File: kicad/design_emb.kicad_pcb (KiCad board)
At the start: 2 copper layers, 110 parts, among them J1 Conn_01x03, J2 Barrel_Jack, J3 USB_A, J4 Conn_01x03, J5 Conn_02x11_Counter_Clockwise, J6 Conn_02x10_Counter_Clockwise, J7 Screw_Terminal_01x02, J8 Screw_Terminal_01x02, K1 SANYOU_SRD_Form_C, K2 SANYOU_SRD_Form_C, Q1 MMBT3904, Q2 MMBT3904, U1 SRX.X.TCT, U10 S25FL116KOXNFIQ-11, U2 SRX.X.TCT, U3 STM32F446ZETx, U4 ICE40HX1K, U5 TLV1117LV33DCYR, U6 TLV1117LV33DCYR, U7 TLV1117LV12DCYR, U8 OMEGA2, U9 RCLAMP0502B

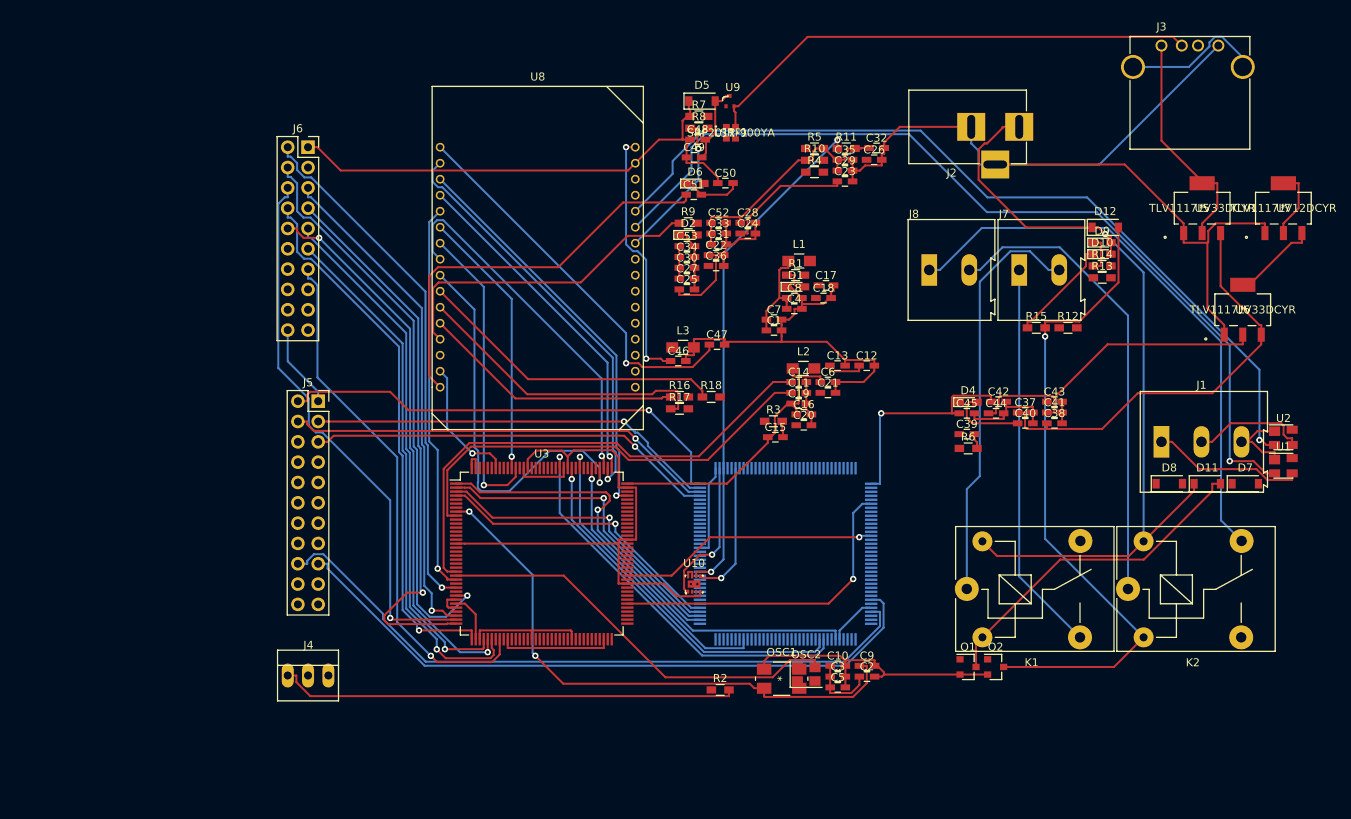
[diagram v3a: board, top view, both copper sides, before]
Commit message: arreglo pines FPGA compatibilidad STM32
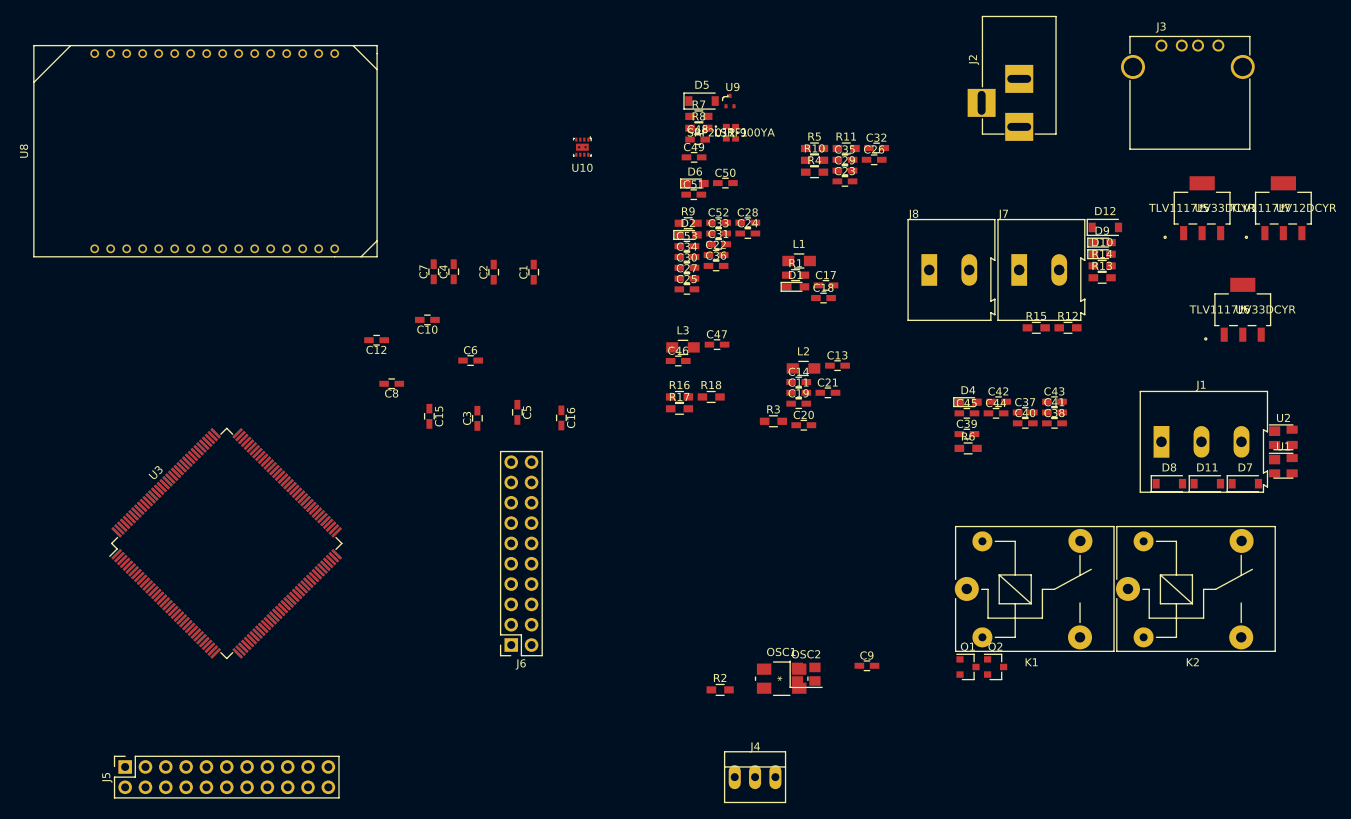
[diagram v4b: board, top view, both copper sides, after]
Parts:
- moved U4 69.9 mm to (52.1, 135.9), turned to 45 degrees
- moved C2 68.8 mm to (85.4, 102.0), turned to 90 degrees
- moved J6 67.2 mm to (87.6, 148.6), turned to 180 degrees
- moved C10 67.1 mm to (77.2, 108.0), turned to 180 degrees
- moved C12 61.3 mm to (70.8, 110.5), turned to 180 degrees
- moved J4 57.3 mm to (115.6, 165.1)
- moved U10 56.4 mm to (96.5, 86.4), turned to 180 degrees
- moved C3 55.4 mm to (83.4, 120.2), turned to 90 degrees
- moved C5 52.8 mm to (88.4, 119.5), turned to 270 degrees
- moved J5 51.7 mm to (39.4, 163.8), turned to 90 degrees
- moved C8 51.5 mm to (72.7, 115.9), turned to 180 degrees
- moved U8 45.0 mm to (35.6, 99.1), turned to 90 degrees
- moved C6 44.7 mm to (82.5, 113.0)
- moved C15 43.3 mm to (77.4, 120.0), turned to 270 degrees
- moved C7 43.0 mm to (77.9, 101.9), turned to 90 degrees
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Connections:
- net /sheet3/FMCNBL0 renamed Net-(U4-Pad112)
- net /sheet3/FMCNBL1 renamed Net-(U4-Pad113)
- J5 pad 10: /sheet3/GPIO18 -> /sheet3/GPIO7
- J5 pad 11: /sheet3/GPIO19 -> /sheet3/GPIO8
- J5 pad 13: /sheet3/GPIO8 -> /sheet3/GPIO10
- J5 pad 14: /sheet3/GPIO7 -> /sheet3/GPIO11
- J5 pad 15: /sheet3/GPIO6 -> /sheet3/GPIO12
- J5 pad 16: /sheet3/GPIO5 -> /sheet3/GPIO13
- J5 pad 17: /sheet3/GPIO4 -> /sheet3/GPIO14
- J5 pad 18: /sheet3/GPIO3 -> /sheet3/GPIO15
- J5 pad 19: /sheet3/GPIO2 -> /sheet3/GPIO16
- J5 pad 2: /sheet3/GPIO10 -> /Sheet4/+3V3_FPGA
- J5 pad 20: /sheet3/GPIO1 -> /sheet3/GPIO17
- J5 pad 21: /sheet3/GPIO0 -> /sheet3/GPIO18
- J5 pad 22: /Sheet4/+3V3_FPGA -> /sheet3/GPIO19
- J5 pad 3: /sheet3/GPIO11 -> /sheet3/GPIO0
- J5 pad 4: /sheet3/GPIO12 -> /sheet3/GPIO1
- J5 pad 5: /sheet3/GPIO13 -> /sheet3/GPIO2
- J5 pad 6: /sheet3/GPIO14 -> /sheet3/GPIO3
- J5 pad 7: /sheet3/GPIO15 -> /sheet3/GPIO4
- J5 pad 8: /sheet3/GPIO16 -> /sheet3/GPIO5
- J5 pad 9: /sheet3/GPIO17 -> /sheet3/GPIO6
- J6 pad 10: /Sheet1/USR9 -> /Sheet1/USR8
- J6 pad 11: /Sheet1/USR10 -> /Sheet1/USR9
- J6 pad 12: /Sheet1/USR11 -> /Sheet1/USR10
- J6 pad 13: /Sheet1/USR12 -> /Sheet1/USR11
- J6 pad 14: /Sheet1/USR13 -> /Sheet1/USR12
- J6 pad 15: /Sheet1/USR14 -> /Sheet1/USR13
- J6 pad 16: /Sheet1/USR15 -> /Sheet1/USR14
- J6 pad 17: /Sheet1/USR16 -> /Sheet1/USR15
- J6 pad 18: /Sheet1/USR17 -> /Sheet1/USR16
- J6 pad 19: /Sheet1/USR18 -> /Sheet1/USR17
- J6 pad 2: /Sheet1/USR1 -> GND
- J6 pad 20: GND -> /Sheet1/USR18
- J6 pad 3: /Sheet1/USR2 -> /Sheet1/USR1
- J6 pad 4: /Sheet1/USR3 -> /Sheet1/USR2
- J6 pad 5: /Sheet1/USR4 -> /Sheet1/USR3
- J6 pad 6: /Sheet1/USR5 -> /Sheet1/USR4
- J6 pad 7: /Sheet1/USR6 -> /Sheet1/USR5
- J6 pad 8: /Sheet1/USR7 -> /Sheet1/USR6
- J6 pad 9: /Sheet1/USR8 -> /Sheet1/USR7
- R10 pad 2: /sheet3/SPI0 -> /Sheet2/SPI0
- R11 pad 1: /sheet3/SPI1 -> /Sheet2/SPI1
- R12 pad 1: Net-(R12-Pad1) -> Net-(Q1-Pad1)
- R13 pad 1: Net-(R13-Pad1) -> Net-(Q2-Pad1)
- U10 pad 1: /sheet3/SPI0 -> /Sheet2/SPI0
- U10 pad 2: /sheet3/SPI2 -> /Sheet2/SPI2
- U10 pad 5: /sheet3/SPI3 -> /Sheet2/SPI3
- U10 pad 6: /sheet3/SPI1 -> /Sheet2/SPI1
- U3 pad 100: Net-(U3-Pad100) -> /Sheet1/USR16
- U3 pad 101: Net-(U3-Pad101) -> /Sheet1/USR17
- U3 pad 102: Net-(U3-Pad102) -> /Sheet1/USR18
- U3 pad 27: /Sheet1/USR1 -> Net-(U3-Pad27)
- U3 pad 28: /Sheet1/USR2 -> Net-(U3-Pad28)
- U3 pad 29: /Sheet1/USR3 -> Net-(U3-Pad29)
- U3 pad 34: /Sheet1/USR4 -> Net-(U3-Pad34)
- U3 pad 35: /Sheet1/USR5 -> Net-(U3-Pad35)
- U3 pad 36: /Sheet1/USR6 -> Net-(U3-Pad36)
- U3 pad 37: /Sheet1/USR7 -> /Sheet1/USR1
- U3 pad 40: /Sheet1/USR8 -> /Sheet1/USR2
- U3 pad 41: /Sheet1/USR9 -> /Sheet1/USR3
- U3 pad 42: /Sheet1/USR10 -> /Sheet1/USR4
- U3 pad 43: /Sheet1/USR11 -> /Sheet1/USR5
- U3 pad 44: /Sheet1/USR12 -> Net-(U3-Pad44)
- U3 pad 46: /Sheet1/USR14 -> Net-(U3-Pad46)
- U3 pad 69: /Sheet1/USR13 -> /Sheet1/USR6
- U3 pad 70: /Sheet1/USR14 -> /Sheet1/USR7
- U3 pad 73: /Sheet1/USR15 -> /Sheet1/USR8
- U3 pad 74: /Sheet1/USR16 -> /Sheet1/USR9
- U3 pad 75: /Sheet1/USR17 -> /Sheet1/USR10
- U3 pad 76: /Sheet1/USR18 -> /Sheet1/USR11
- U3 pad 96: Net-(U3-Pad96) -> /Sheet1/USR12
- U3 pad 97: Net-(U3-Pad97) -> /Sheet1/USR13
- U3 pad 98: Net-(U3-Pad98) -> /Sheet1/USR14
- U3 pad 99: Net-(U3-Pad99) -> /Sheet1/USR15
- U4 pad 1: /sheet3/GPIO0 -> /Sheet1/FMCA23
- U4 pad 10: /sheet3/GPIO7 -> Net-(U4-Pad10)
- U4 pad 102: /Sheet1/FMCA22 -> Net-(U4-Pad102)
- U4 pad 104: /Sheet1/FMCA21 -> Net-(U4-Pad104)
- U4 pad 105: /Sheet1/FMCA20 -> Net-(U4-Pad105)
- U4 pad 106: /Sheet1/FMCA19 -> Net-(U4-Pad106)
- U4 pad 107: /Sheet1/FMCA23 -> Net-(U4-Pad107)
- U4 pad 11: /sheet3/GPIO8 -> Net-(U4-Pad11)
- U4 pad 114: Net-(U4-Pad114) -> /Sheet1/FMCAD3
- U4 pad 115: /Sheet1/CTRL0 -> /Sheet1/FMCAD2
- U4 pad 116: /Sheet1/CTRL1 -> Net-(U4-Pad116)
- U4 pad 117: Net-(U4-Pad117) -> /Sheet1/CTRL1
- U4 pad 118: Net-(U4-Pad118) -> /Sheet1/CTRL2
- U4 pad 119: Net-(U4-Pad119) -> /Sheet1/CTRL3
- U4 pad 12: /sheet3/GPIO9 -> Net-(U4-Pad12)
- U4 pad 120: Net-(U4-Pad120) -> /Sheet1/CTRL4
- U4 pad 121: Net-(U4-Pad121) -> /Sheet1/CTRL5
- U4 pad 134: /Sheet1/CTRL2 -> Net-(U4-Pad134)
- U4 pad 135: /Sheet1/CTRL3 -> Net-(U4-Pad135)
- U4 pad 136: /Sheet1/CTRL4 -> Net-(U4-Pad136)
- U4 pad 137: /Sheet1/CTRL5 -> /Sheet1/CTRL0
- U4 pad 138: /Sheet1/FMCAD3 -> Net-(U4-Pad138)
- U4 pad 139: /Sheet1/FMCAD2 -> Net-(U4-Pad139)
- U4 pad 141: Net-(U4-Pad141) -> /Sheet1/FMCNBL0
- U4 pad 142: Net-(U4-Pad142) -> /Sheet1/FMCNBL1
- U4 pad 19: Net-(U4-Pad19) -> /sheet3/GPIO0
- U4 pad 2: /sheet3/GPIO1 -> /Sheet1/FMCA22
- U4 pad 22: /Sheet1/FMCAD1 -> /sheet3/GPIO1
- U4 pad 23: /Sheet1/FMCAD0 -> /sheet3/GPIO2
- U4 pad 24: Net-(U4-Pad24) -> /sheet3/GPIO3
- U4 pad 25: /Sheet1/FMCA18 -> /sheet3/GPIO4
- U4 pad 26: /Sheet1/FMCA17 -> /sheet3/GPIO5
- U4 pad 28: /Sheet1/FMCA16 -> /sheet3/GPIO6
- U4 pad 29: /Sheet1/FMCAD15 -> /sheet3/GPIO7
- U4 pad 3: /sheet3/GPIO2 -> /Sheet1/FMCA19
- U4 pad 31: /Sheet1/FMCAD14 -> /sheet3/GPIO8
- U4 pad 32: /Sheet1/FMCAD13 -> /sheet3/GPIO9
- U4 pad 33: Net-(U4-Pad33) -> /sheet3/GPIO10
- U4 pad 34: Net-(U4-Pad34) -> /sheet3/GPIO11
- U4 pad 37: Net-(U4-Pad37) -> /sheet3/GPIO12
- U4 pad 38: Net-(U4-Pad38) -> /sheet3/GPIO13
- U4 pad 39: Net-(U4-Pad39) -> /sheet3/GPIO14
- U4 pad 4: /sheet3/GPIO3 -> /Sheet1/FMCA20
- U4 pad 41: /Sheet1/FMCAD12 -> /sheet3/GPIO15
- U4 pad 42: /Sheet1/FMCAD11 -> /sheet3/GPIO16
- U4 pad 43: /Sheet1/FMCAD10 -> /sheet3/GPIO17
- U4 pad 44: /Sheet1/FMCAD9 -> /sheet3/GPIO18
- U4 pad 45: /Sheet1/FMCAD8 -> /sheet3/GPIO19
- U4 pad 47: /Sheet1/FMCAD7 -> Net-(U4-Pad47)
- U4 pad 48: /Sheet1/FMCAD6 -> Net-(U4-Pad48)
- U4 pad 49: /Sheet1/FMCAD5 -> Net-(U4-Pad49)
- U4 pad 50: /Sheet1/FMCAD4 -> Net-(U4-Pad50)
- U4 pad 56: Net-(U4-Pad56) -> /Sheet1/FMCAD4
- U4 pad 58: Net-(U4-Pad58) -> /Sheet1/FMCAD5
- U4 pad 60: Net-(U4-Pad60) -> /Sheet1/FMCAD6
- U4 pad 61: Net-(U4-Pad61) -> /Sheet1/FMCAD7
- U4 pad 62: Net-(U4-Pad62) -> /Sheet1/FMCAD8
- U4 pad 67: /sheet3/SPI3 -> /Sheet2/SPI3
- U4 pad 68: /sheet3/SPI2 -> /Sheet2/SPI2
- U4 pad 7: /sheet3/GPIO4 -> /Sheet1/FMCA21
- U4 pad 70: /sheet3/SPI1 -> /Sheet2/SPI1
- U4 pad 71: /sheet3/SPI0 -> /Sheet2/SPI0
- U4 pad 73: /sheet3/GPIO10 -> /Sheet1/FMCAD9
- U4 pad 74: /sheet3/GPIO11 -> /Sheet1/FMCAD10
- U4 pad 75: /sheet3/GPIO12 -> /Sheet1/FMCAD11
- U4 pad 76: /sheet3/GPIO13 -> /Sheet1/FMCAD12
- U4 pad 78: /sheet3/GPIO14 -> /Sheet1/FMCAD13
- U4 pad 79: /sheet3/GPIO15 -> /Sheet1/FMCAD14
- U4 pad 8: /sheet3/GPIO5 -> Net-(U4-Pad8)
- U4 pad 80: /sheet3/GPIO16 -> /Sheet1/FMCAD15
- U4 pad 81: /sheet3/GPIO17 -> /Sheet1/FMCA16
- U4 pad 87: /sheet3/GPIO18 -> /Sheet1/FMCAD0
- U4 pad 88: /sheet3/GPIO19 -> /Sheet1/FMCAD1
- U4 pad 9: /sheet3/GPIO6 -> Net-(U4-Pad9)
- U4 pad 90: Net-(U4-Pad90) -> /Sheet1/FMCA17
- U4 pad 91: Net-(U4-Pad91) -> /Sheet1/FMCA18
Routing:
- net GND: track 367.4 -> 0.00 mm
- net VDD: track 194.0 -> 0.00 mm
- net /SERIAL_RX: track 112.5 -> 0.00 mm, vias 1 -> 0
- net /SERIAL_TX: track 106.4 -> 0.00 mm, vias 1 -> 0
- net +5VA: track 103.7 -> 0.00 mm, vias 1 -> 0
- net /Sheet4/+3V3_FPGA: track 99.5 -> 0.00 mm
- net /sheet3/GPIO3: track 84.1 -> 0.00 mm
- net /sheet3/GPIO4: track 83.1 -> 0.00 mm
- net Net-(D12-Pad2): track 81.7 -> 0.00 mm, vias 1 -> 0
- net /Sheet1/USR3: track 71.5 -> 0.00 mm, vias 1 -> 0
- net /Sheet1/OSC32_IN: track 71.1 -> 0.00 mm, vias 2 -> 0
- net Net-(J8-Pad1): track 70.5 -> 0.00 mm
- net /Sheet1/USR6: track 69.8 -> 0.00 mm, vias 1 -> 0
- net /Sheet1/USR5: track 69.1 -> 0.00 mm, vias 1 -> 0
- net /Sheet1/USR9: track 68.8 -> 0.00 mm, vias 2 -> 0
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
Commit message: design_emb.kicad_pcb
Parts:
- moved D7 108.1 mm to (72.4, 143.5), turned to 180 degrees
- moved D8 98.3 mm to (72.4, 141.0), turned to 180 degrees
- moved C17 98.3 mm to (43.2, 154.9), turned to 270 degrees
- moved C9 97.8 mm to (34.3, 148.6), turned to 90 degrees
- moved C14 96.4 mm to (35.6, 154.9), turned to 90 degrees
- moved C11 85.2 mm to (44.5, 148.6), turned to 270 degrees
- moved OSC2 85.1 mm to (39.4, 154.8)
- moved J2 84.2 mm to (104.1, 153.7)
- moved OSC1 82.2 mm to (39.4, 148.6)
- moved D11 63.9 mm to (116.0, 153.7)
- moved J4 43.8 mm to (72.4, 157.5), turned to 90 degrees
- moved R2 40.5 mm to (73.7, 160.0), turned to 180 degrees
- moved J1 38.2 mm to (171.4, 161.3)
- moved LSRF1 24.9 mm to (90.9, 78.7)
- moved U9 24.8 mm to (90.9, 74.3)
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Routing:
- net /sheet3/GPIO1: track 0.00 -> 21.3 mm
- net /sheet3/GPIO3: track 0.00 -> 20.5 mm
- net /sheet3/GPIO5: track 0.00 -> 19.8 mm
- net /sheet3/GPIO17: track 0.00 -> 19.5 mm
- net /sheet3/GPIO0: track 0.00 -> 19.3 mm
- net /sheet3/GPIO7: track 0.00 -> 19.1 mm
- net /sheet3/GPIO9: track 0.00 -> 18.5 mm
- net /sheet3/GPIO11: track 0.00 -> 18.3 mm
- net /sheet3/GPIO15: track 0.00 -> 18.2 mm
- net /sheet3/GPIO2: track 0.00 -> 17.5 mm
- net /sheet3/GPIO18: track 0.00 -> 17.3 mm
- net /sheet3/GPIO4: track 0.00 -> 17.0 mm
- net /sheet3/GPIO13: track 0.00 -> 16.5 mm
- net /sheet3/GPIO6: track 0.00 -> 16.4 mm
- net /sheet3/GPIO16: track 0.00 -> 15.8 mm
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
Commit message: ruteo
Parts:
- moved C14 9.16 mm to (43.2, 149.9), turned to 45 degrees
- moved C9 8.98 mm to (33.0, 139.7), turned to 45 degrees
- moved OSC2 6.75 mm to (45.7, 152.4), turned to 315 degrees
- moved J6 5.80 mm to (87.6, 148.3)
- moved OSC1 5.68 mm to (36.8, 143.5), turned to 315 degrees
- moved C17 5.08 mm to (48.3, 154.9), turned to 225 degrees
- moved C11 4.02 mm to (40.6, 147.3), turned to 225 degrees
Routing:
- net /Sheet1/OSC32_IN: track 0.00 -> 10.9 mm
- net /Sheet1/OSC_OUT: track 0.00 -> 10.5 mm
- net /Sheet1/OSC_IN: track 0.00 -> 9.50 mm
- net /Sheet1/OSC32_OUT: track 0.00 -> 8.19 mm
- net /Sheet1/FMCAD9: track 0.00 -> 7.53 mm, vias 0 -> 1
- net /Sheet1/FMCAD10: track 0.00 -> 7.34 mm, vias 0 -> 1
- net /Sheet1/FMCAD12: track 0.00 -> 7.16 mm, vias 0 -> 1
- net /Sheet1/FMCAD11: track 0.00 -> 7.13 mm, vias 0 -> 1
- net /Sheet1/FMCA22: track 11.1 -> 4.38 mm
- net /Sheet1/FMCA21: track 0.00 -> 5.85 mm, vias 0 -> 1
- net /Sheet1/FMCAD8: track 0.00 -> 5.62 mm, vias 0 -> 1
- net /Sheet1/FMCAD6: track 0.00 -> 5.26 mm, vias 0 -> 1
- net /Sheet1/FMCAD4: track 0.00 -> 4.20 mm, vias 0 -> 1
- net /Sheet1/FMCAD5: track 0.00 -> 3.86 mm, vias 0 -> 1
- net /Sheet1/FMCAD7: track 0.00 -> 3.83 mm, vias 0 -> 1
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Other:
- net class signals added: clearance 0.15, trace_width 0.15, via_dia 0.8, via_drill 0.4
- rule trace_min: 0.2 -> 0.15

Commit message: ruteo
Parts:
- moved K1 146.1 mm to (267.4, 113.5), turned to 180 degrees
- moved J2 135.8 mm to (206.6, 64.6)
- moved K2 132.1 mm to (267.6, 95.1), turned to 180 degrees
- moved D7 105.1 mm to (177.2, 150.6)
- moved D8 105.0 mm to (177.3, 145.9)
- moved J4 101.2 mm to (172.7, 171.5)
- moved R2 98.8 mm to (172.4, 160.1)
- moved C4 88.9 mm to (113.4, 19.3)
- moved C7 88.9 mm to (110.9, 19.3)
- moved C1 88.9 mm to (123.4, 19.4)
- moved C10 88.9 mm to (110.2, 25.4)
- moved C12 88.9 mm to (103.8, 27.9)
- moved C15 88.9 mm to (110.4, 37.4)
- moved C16 88.9 mm to (126.9, 37.6)
- moved C2 88.9 mm to (118.4, 19.4)
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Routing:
- net /Sheet1/USR18: track 0.00 -> 49.6 mm, vias 0 -> 1
- net /Sheet1/USR2: track 0.00 -> 48.4 mm, vias 0 -> 1
- net /Sheet1/USR16: track 0.00 -> 47.9 mm, vias 0 -> 1
- net /Sheet1/USR4: track 0.00 -> 47.8 mm, vias 0 -> 1
- net /sheet3/GPIO19: track 9.72 -> 57.0 mm
- net /Sheet1/USR14: track 0.00 -> 46.9 mm, vias 0 -> 1
- net /Sheet1/USR1: track 0.00 -> 46.6 mm, vias 0 -> 1
- net /Sheet1/USR17: track 0.00 -> 45.4 mm, vias 0 -> 1
- net /Sheet1/USR12: track 0.00 -> 45.4 mm, vias 0 -> 1
- net /Sheet1/USR3: track 0.00 -> 45.0 mm, vias 0 -> 1
- net /Sheet1/USR5: track 0.00 -> 44.3 mm, vias 0 -> 1
- net /Sheet1/USR15: track 0.00 -> 44.3 mm, vias 0 -> 1
- net /Sheet1/USR13: track 0.00 -> 43.0 mm, vias 0 -> 1
- net /sheet3/GPIO16: track 15.8 -> 51.7 mm
- net /Sheet1/USR10: track 0.00 -> 35.9 mm, vias 0 -> 1
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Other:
- net class signals: via_dia 0.8 -> 0.6; via_drill 0.4 -> 0.3

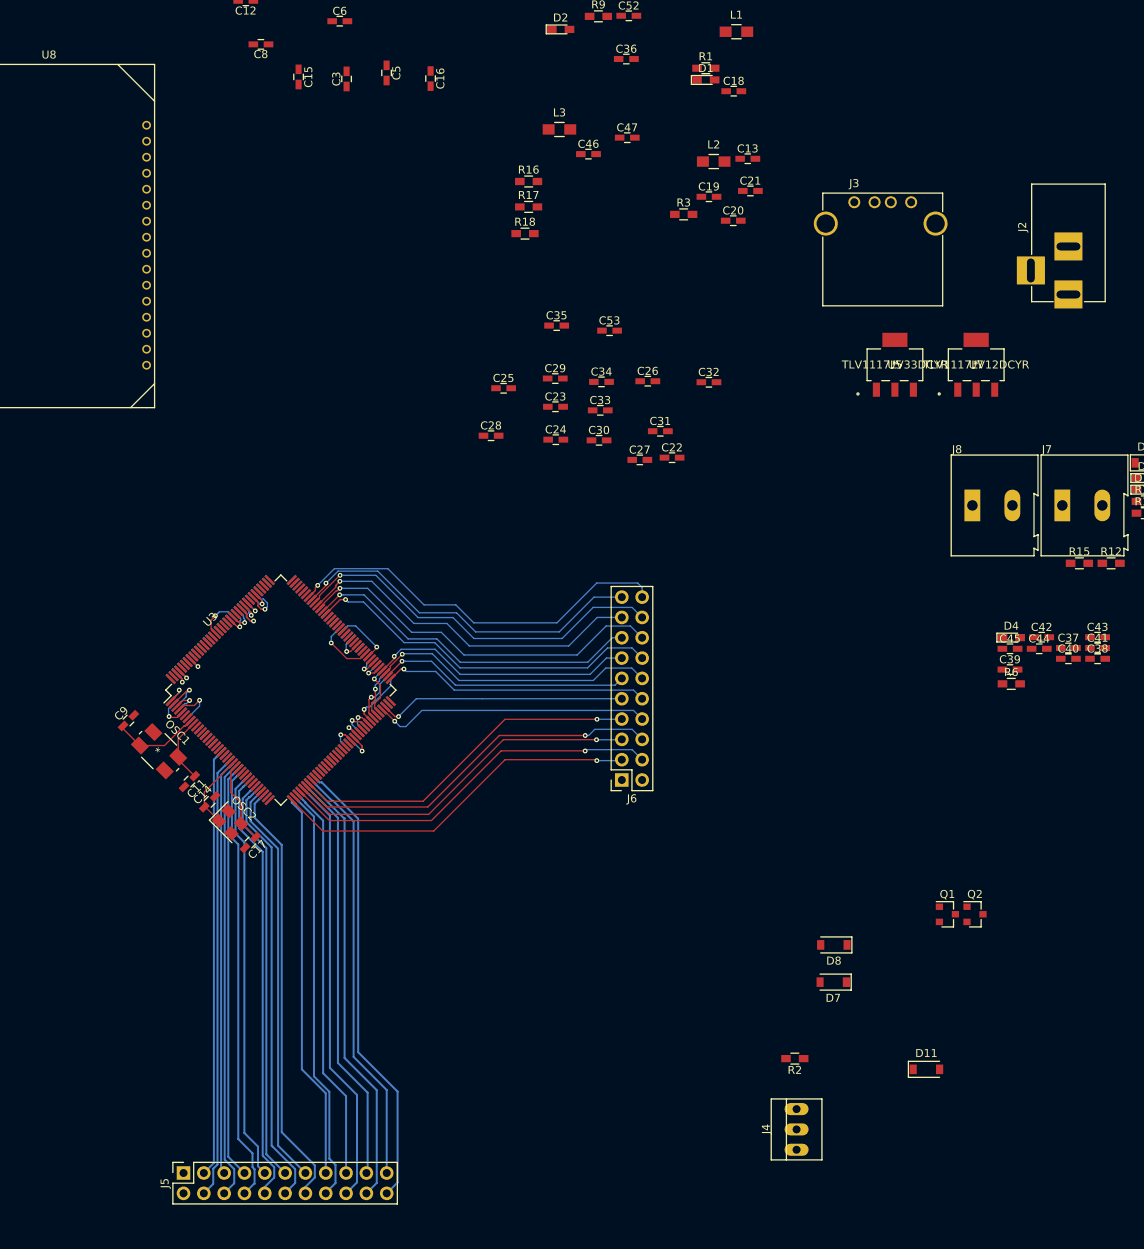
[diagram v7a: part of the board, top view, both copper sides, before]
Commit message: footprint sw_push
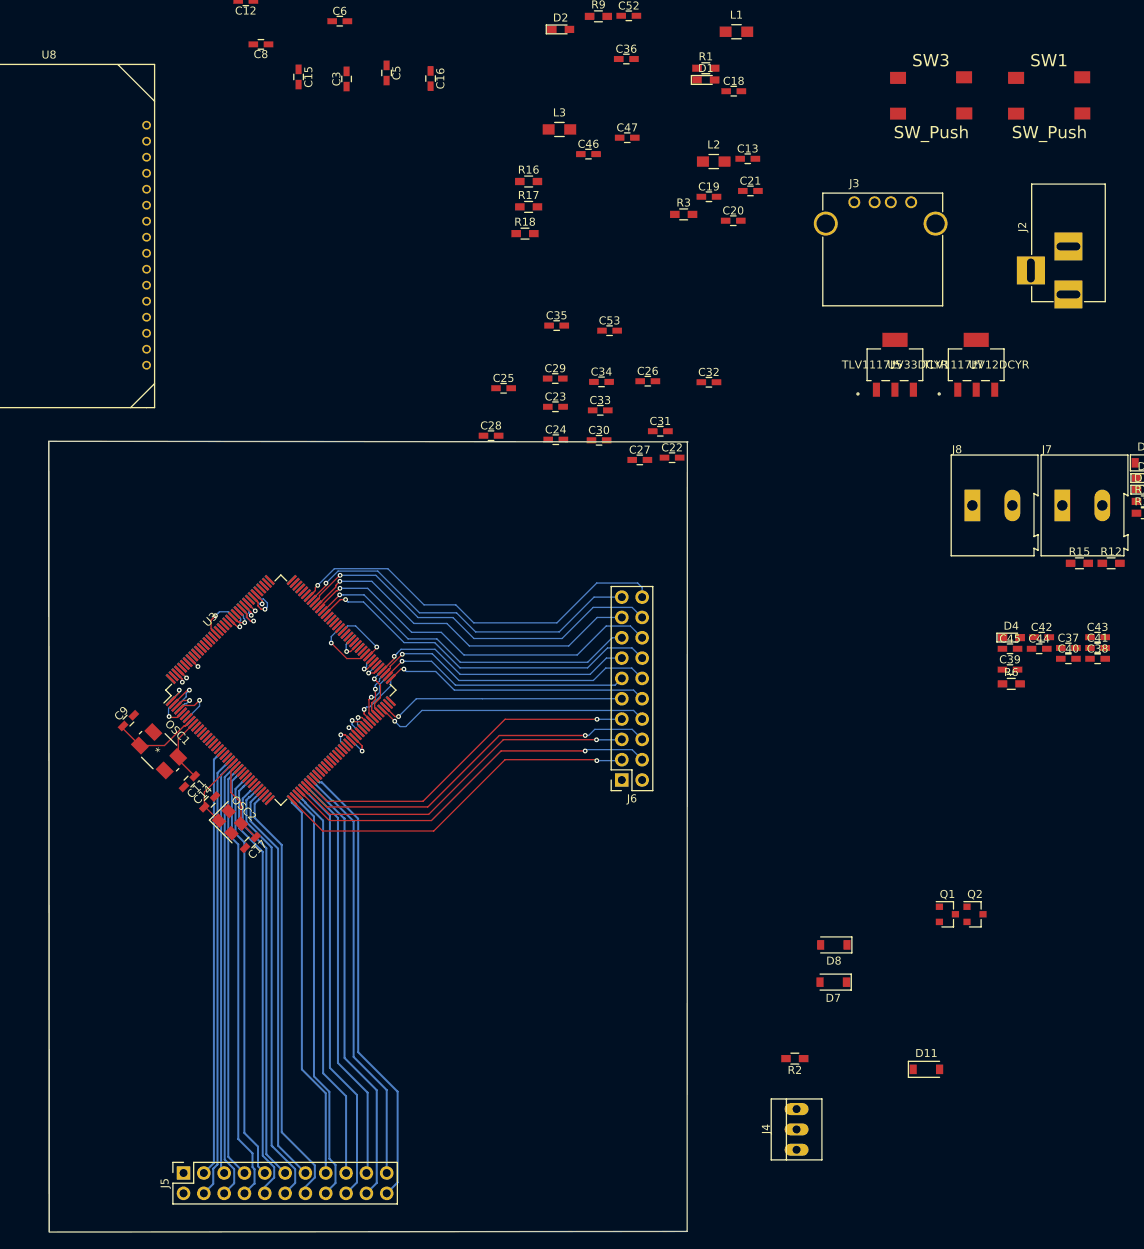
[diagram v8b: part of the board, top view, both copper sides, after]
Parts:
- added SW1: SW_Push, Switch:TACTILE_SWITCH_6mm, F.Cu at (204.2, 39.8)
- added SW3: SW_Push, Switch:TACTILE_SWITCH_6mm, F.Cu at (189.5, 39.8)
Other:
- board outline added: 79.9 x 98.8 mm
